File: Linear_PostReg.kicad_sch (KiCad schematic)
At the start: 45 parts, among them Q301 BCP56, Q302 BSS138, Q303 TIP125, Q304 BCP56, U301 TLV4387PWR, U302 LMV331

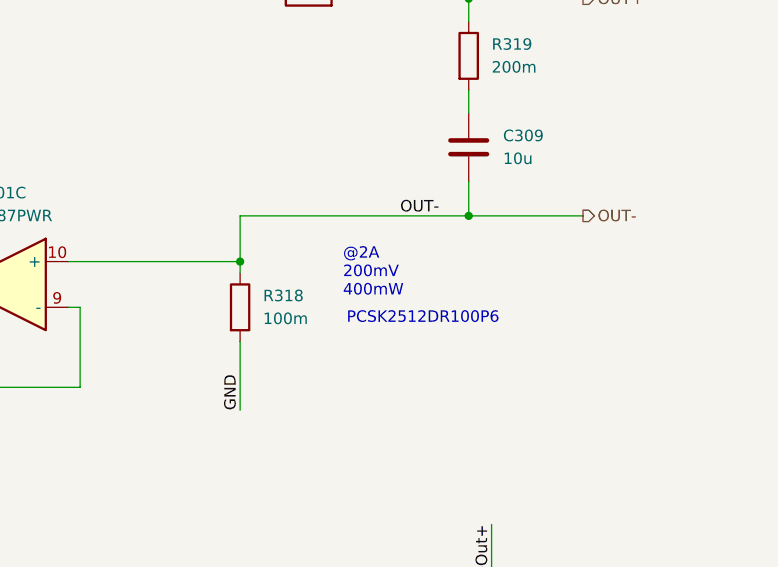
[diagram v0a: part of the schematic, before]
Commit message: add adc and dac estimate
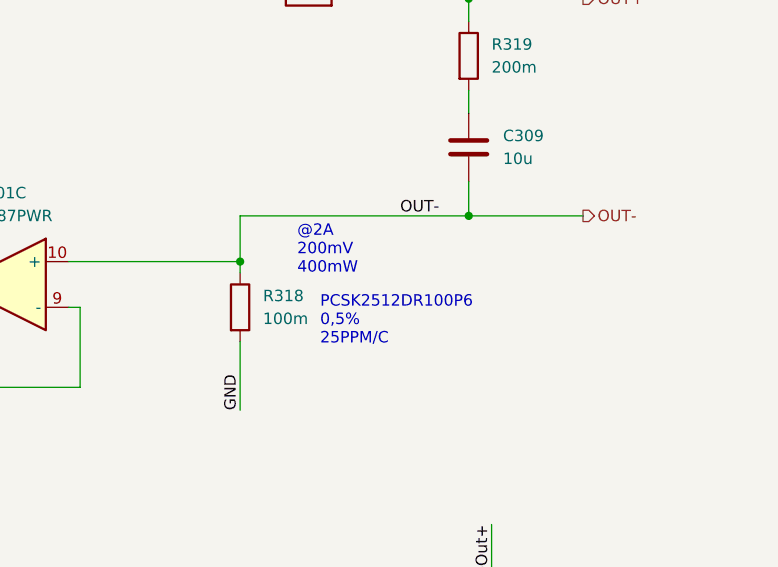
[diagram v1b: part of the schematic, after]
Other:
- note added: "PCSK2512DR100P6 0,5% 25PPM/C"
- note removed: "PCSK2512DR100P6"
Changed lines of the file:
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@@
 	(text "@2A\n200mV\n400mW"
 		(exclude_from_sim no)
-		(at 224.79 88.9 0)
+		(at 219.71 86.36 0)
 		(effects
 			(font
@@
 		)
 	)
-	(text "PCSK2512DR100P6"
+	(text "PCSK2512DR100P6\n0,5%\n25PPM/C"
 		(exclude_from_sim no)
-		(at 233.68 93.98 0)
+		(at 222.25 91.44 0)
 		(effects
 			(font
 				(size 1.27 1.27)
 			)
+			(justify left top)
 		)
 	)
@@
 			)
 		)
-		(property "Datasheet" ""
+		(property "Datasheet" "https://s.resistor.today/shop/products/epdf/PCSK.pdf"
 			(at 213.36 92.71 0)
 			(hide yes)

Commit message: add diodes for clamping
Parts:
- added C1004, C1014: 100p, Capacitor_SMD:C_0603_1608Metric, symbol Device:C
- added D1003, D1004, D1006: 1N4148WS, Diode_SMD:D_SOD-323, symbol Diode:1N4148WS
- added D1005: MM3Z4V7T1G, Diode_SMD:D_SOD-323, symbol Device:D_Zener
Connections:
- net Base_drive: now also D1005.2 (A)
- net CC_loop: now also C1004.2, D1003.2 (A)
- net CV_loop: now also C1014.2, D1004.2 (A)
- net PreReg: now also D1005.1 (K)
- net preFuseOut+: now also D1006.2 (A); no longer Q304.2 (C), Q304.4 (C)
- net at C303.1, R301.2, U301.2 (-): now also C1014.1, D1004.1 (K)
- net at C304.1, R302.2, U301.6 (-): now also C1004.1, D1003.1 (K)
- new net: D1006.1 (K), Q304.2 (C), Q304.4 (C)
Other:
- note added: "4,7V Zener"
- note added: "PreReg = Vout + 2,2V"
- note removed: "PreReg = Vout + 1,7V"
- moved on the sheet: C303, C304, C305, C306, C308, C310, Q304, R301, R302, R303, R304, R306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
